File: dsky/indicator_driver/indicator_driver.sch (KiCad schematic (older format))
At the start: 0 parts

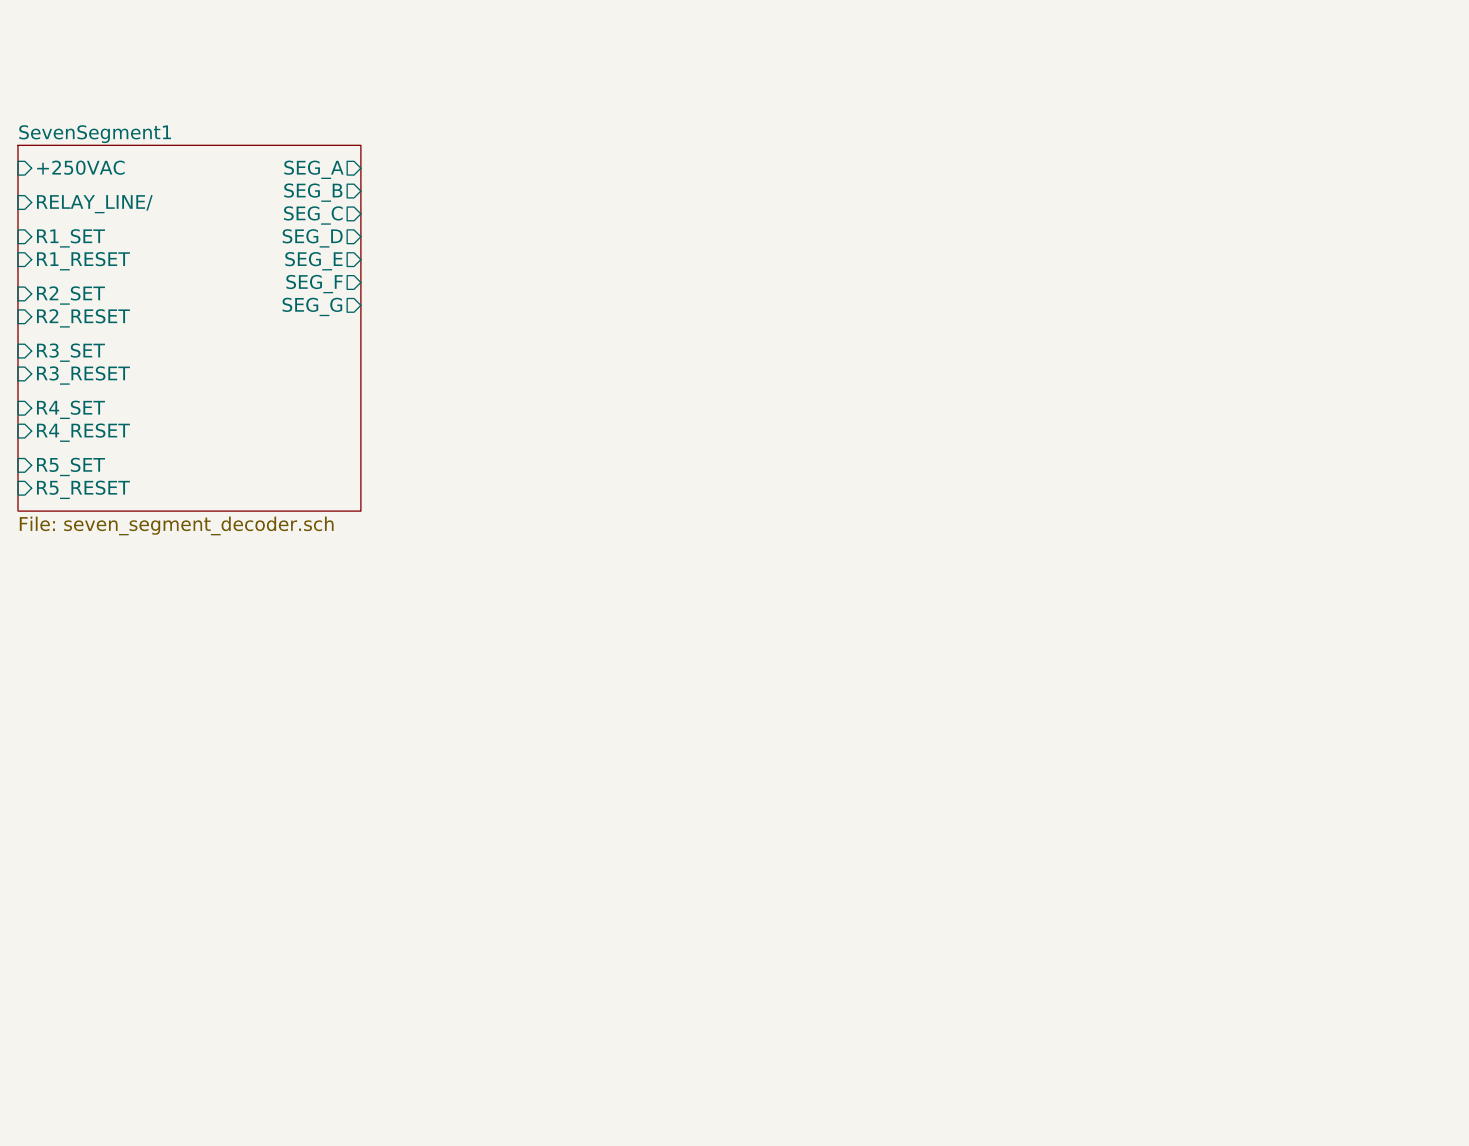
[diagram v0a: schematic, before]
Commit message: New (original) seven-segment decoder, taken from the Apollo 12 Mission Report
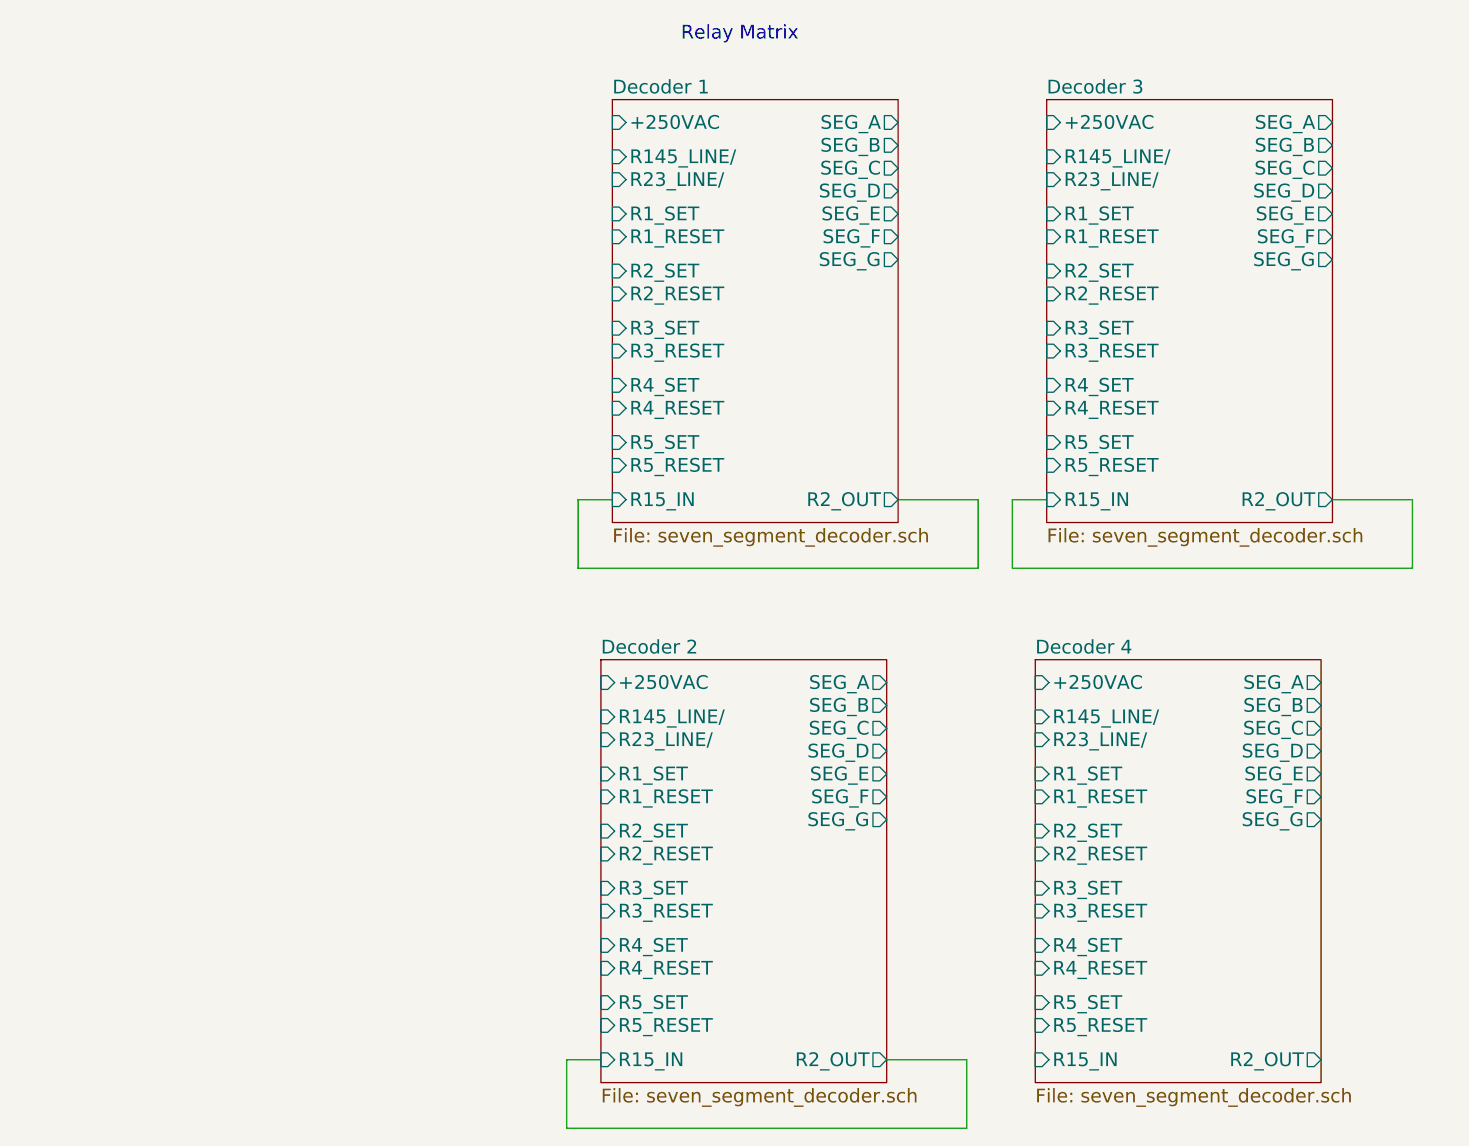
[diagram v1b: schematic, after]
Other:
- note added: "Relay Matrix"
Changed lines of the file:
@@
 $Descr A4 11693 8268
 encoding utf-8
-Sheet 1 2
+Sheet 1 5
 Title ""
 Date ""
@@
 $EndDescr
 $Sheet
-S 1650 1150 1500 1600
+S 4250 950  1250 1850
 U 57369BCB
-F0 "SevenSegment1" 60
+F0 "Decoder 1" 60
 F1 "seven_segment_decoder.sch" 60
-F2 "+250VAC" I L 1650 1250 60
-F3 "SEG_A" O R 3150 1250 60
-F4 "SEG_B" O R 3150 1350 60
-F5 "SEG_D" O R 3150 1550 60
-F6 "SEG_G" O R 3150 1850 60
-F7 "SEG_F" O R 3150 1750 60
-F8 "SEG_C" O R 3150 1450 60
-F9 "SEG_E" O R 3150 1650 60
-F10 "R5_SET" I L 1650 2550 60
-F11 "R5_RESET" I L 1650 2650 60
-F12 "R4_SET" I L 1650 2300 60
-F13 "R4_RESET" I L 1650 2400 60
-F14 "R3_SET" I L 1650 2050 60
-F15 "R3_RESET" I L 1650 2150 60
-F16 "R2_SET" I L 1650 1800 60
-F17 "R2_RESET" I L 1650 1900 60
-F18 "R1_SET" I L 1650 1550 60
-F19 "R1_RESET" I L 1650 1650 60
-F20 "RELAY_LINE/" I L 1650 1400 60
+F2 "+250VAC" I L 4250 1050 60
+F3 "SEG_A" O R 5500 1050 60
+F4 "SEG_B" O R 5500 1150 60
+F5 "SEG_D" O R 5500 1350 60
+F6 "SEG_G" O R 5500 1650 60
+F7 "SEG_F" O R 5500 1550 60
+F8 "SEG_C" O R 5500 1250 60
+F9 "SEG_E" O R 5500 1450 60
+F10 "R5_SET" I L 4250 2450 60
+F11 "R5_RESET" I L 4250 2550 60
+F12 "R4_SET" I L 4250 2200 60
+F13 "R4_RESET" I L 4250 2300 60
+F14 "R3_SET" I L 4250 1950 60
+F15 "R3_RESET" I L 4250 2050 60
+F16 "R2_SET" I L 4250 1700 60
+F17 "R2_RESET" I L 4250 1800 60
+F18 "R1_SET" I L 4250 1450 60
+F19 "R1_RESET" I L 4250 1550 60
+F20 "R145_LINE/" I L 4250 1200 60
+F21 "R23_LINE/" I L 4250 1300 60
+F22 "R2_OUT" O R 5500 2700 60
+F23 "R15_IN" I L 4250 2700 60
+$EndSheet
+Wire Wire Line
+	5500 2700 5850 2700
+Wire Wire Line
+	5850 2700 5850 3000
+Wire Wire Line
+	5850 3000 4100 3000
+Wire Wire Line
+	4100 3000 4100 2700
+Wire Wire Line
+	4100 2700 4250 2700
+Text Notes 4550 700  0    60   ~ 0
+Relay Matrix
+$Sheet
+S 4200 3400 1250 1850
+U 5823C123
+F0 "Decoder 2" 60
+F1 "seven_segment_decoder.sch" 60
+F2 "+250VAC" I L 4200 3500 60
+F3 "SEG_A" O R 5450 3500 60
+F4 "SEG_B" O R 5450 3600 60
+F5 "SEG_D" O R 5450 3800 60
+F6 "SEG_G" O R 5450 4100 60
+F7 "SEG_F" O R 5450 4000 60
+F8 "SEG_C" O R 5450 3700 60
+F9 "SEG_E" O R 5450 3900 60
+F10 "R5_SET" I L 4200 4900 60
+F11 "R5_RESET" I L 4200 5000 60
+F12 "R4_SET" I L 4200 4650 60
+F13 "R4_RESET" I L 4200 4750 60
+F14 "R3_SET" I L 4200 4400 60
+F15 "R3_RESET" I L 4200 4500 60
+F16 "R2_SET" I L 4200 4150 60
+F17 "R2_RESET" I L 4200 4250 60
+F18 "R1_SET" I L 4200 3900 60
+F19 "R1_RESET" I L 4200 4000 60
+F20 "R145_LINE/" I L 4200 3650 60
+F21 "R23_LINE/" I L 4200 3750 60
+F22 "R2_OUT" O R 5450 5150 60
+F23 "R15_IN" I L 4200 5150 60
+$EndSheet
+Wire Wire Line
+	5450 5150 5800 5150
+Wire Wire Line
+	5800 5150 5800 5450
+Wire Wire Line
+	5800 5450 4050 5450
+Wire Wire Line
+	4050 5450 4050 5150
+Wire Wire Line
+	4050 5150 4200 5150
+$Sheet
+S 6150 950  1250 1850
+U 582563A0
+F0 "Decoder 3" 60
+F1 "seven_segment_decoder.sch" 60
+F2 "+250VAC" I L 6150 1050 60
+F3 "SEG_A" O R 7400 1050 60
+F4 "SEG_B" O R 7400 1150 60
+F5 "SEG_D" O R 7400 1350 60
+F6 "SEG_G" O R 7400 1650 60
+F7 "SEG_F" O R 7400 1550 60
+F8 "SEG_C" O R 7400 1250 60
+F9 "SEG_E" O R 7400 1450 60
+F10 "R5_SET" I L 6150 2450 60
+F11 "R5_RESET" I L 6150 2550 60
+F12 "R4_SET" I L 6150 2200 60
+F13 "R4_RESET" I L 6150 2300 60
+F14 "R3_SET" I L 6150 1950 60
+F15 "R3_RESET" I L 6150 2050 60
+F16 "R2_SET" I L 6150 1700 60
+F17 "R2_RESET" I L 6150 1800 60
+F18 "R1_SET" I L 6150 1450 60
+F19 "R1_RESET" I L 6150 1550 60
+F20 "R145_LINE/" I L 6150 1200 60
+F21 "R23_LINE/" I L 6150 1300 60
+F22 "R2_OUT" O R 7400 2700 60
+F23 "R15_IN" I L 6150 2700 60
+$EndSheet
+Wire Wire Line
+	7400 2700 7750 2700
+Wire Wire Line
+	7750 2700 7750 3000
+Wire Wire Line
+	7750 3000 6000 3000
+Wire Wire Line
+	6000 3000 6000 2700
+Wire Wire Line
+	6000 2700 6150 2700
+$Sheet
+S 6100 3400 1250 1850
+U 582563BD
+F0 "Decoder 4" 60
+F1 "seven_segment_decoder.sch" 60
+F2 "+250VAC" I L 6100 3500 60
+F3 "SEG_A" O R 7350 3500 60
+F4 "SEG_B" O R 7350 3600 60
+F5 "SEG_D" O R 7350 3800 60
+F6 "SEG_G" O R 7350 4100 60
+F7 "SEG_F" O R 7350 4000 60
+F8 "SEG_C" O R 7350 3700 60
+F9 "SEG_E" O R 7350 3900 60
+F10 "R5_SET" I L 6100 4900 60
+F11 "R5_RESET" I L 6100 5000 60
+F12 "R4_SET" I L 6100 4650 60
+F13 "R4_RESET" I L 6100 4750 60
+F14 "R3_SET" I L 6100 4400 60
+F15 "R3_RESET" I L 6100 4500 60
+F16 "R2_SET" I L 6100 4150 60
+F17 "R2_RESET" I L 6100 4250 60
+F18 "R1_SET" I L 6100 3900 60
+F19 "R1_RESET" I L 6100 4000 60
+F20 "R145_LINE/" I L 6100 3650 60
+F21 "R23_LINE/" I L 6100 3750 60
+F22 "R2_OUT" O R 7350 5150 60
+F23 "R15_IN" I L 6100 5150 60
 $EndSheet
 $EndSCHEMATC

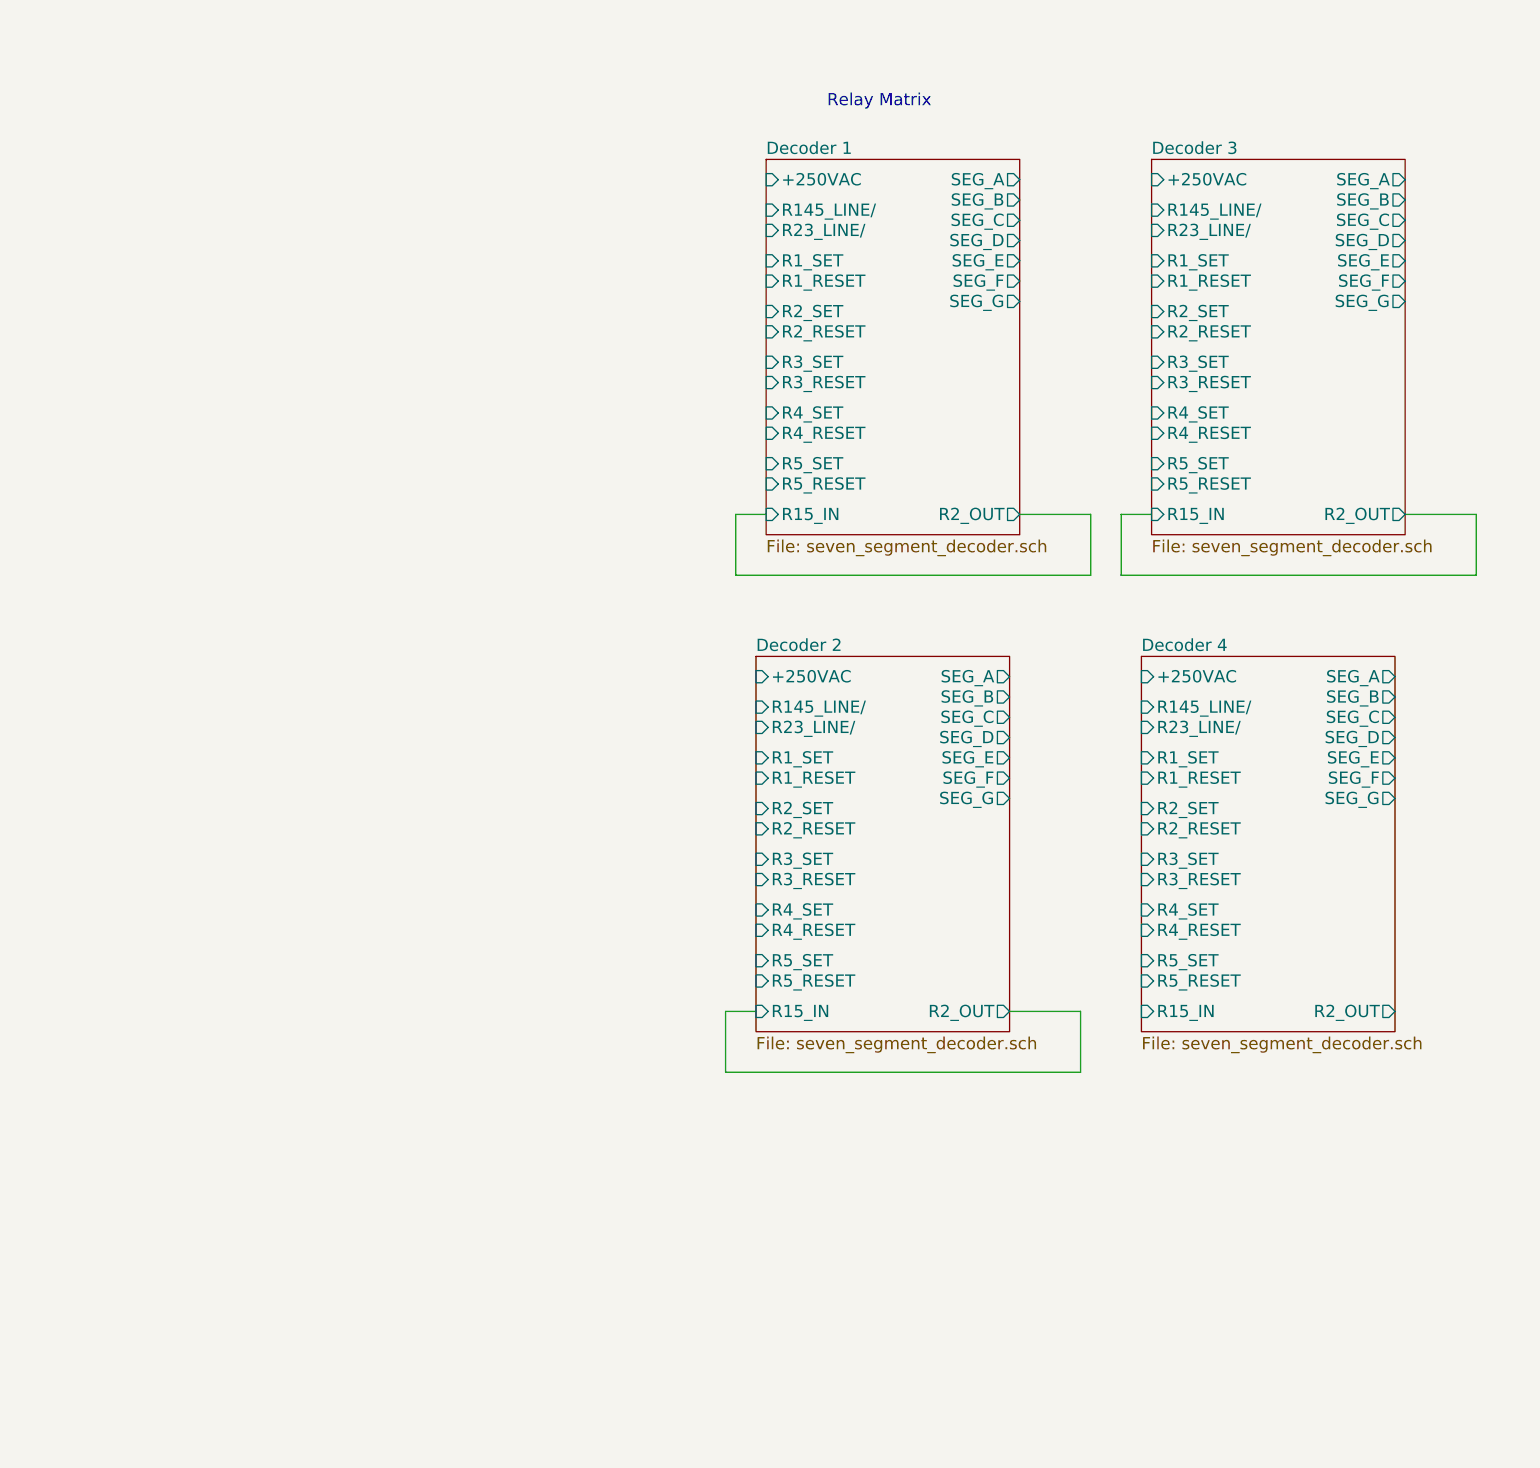
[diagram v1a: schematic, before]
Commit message: Added in the rest of the IDM hardware. Values and diode matrix design still need to be finalized. Working on wiring everything up now.
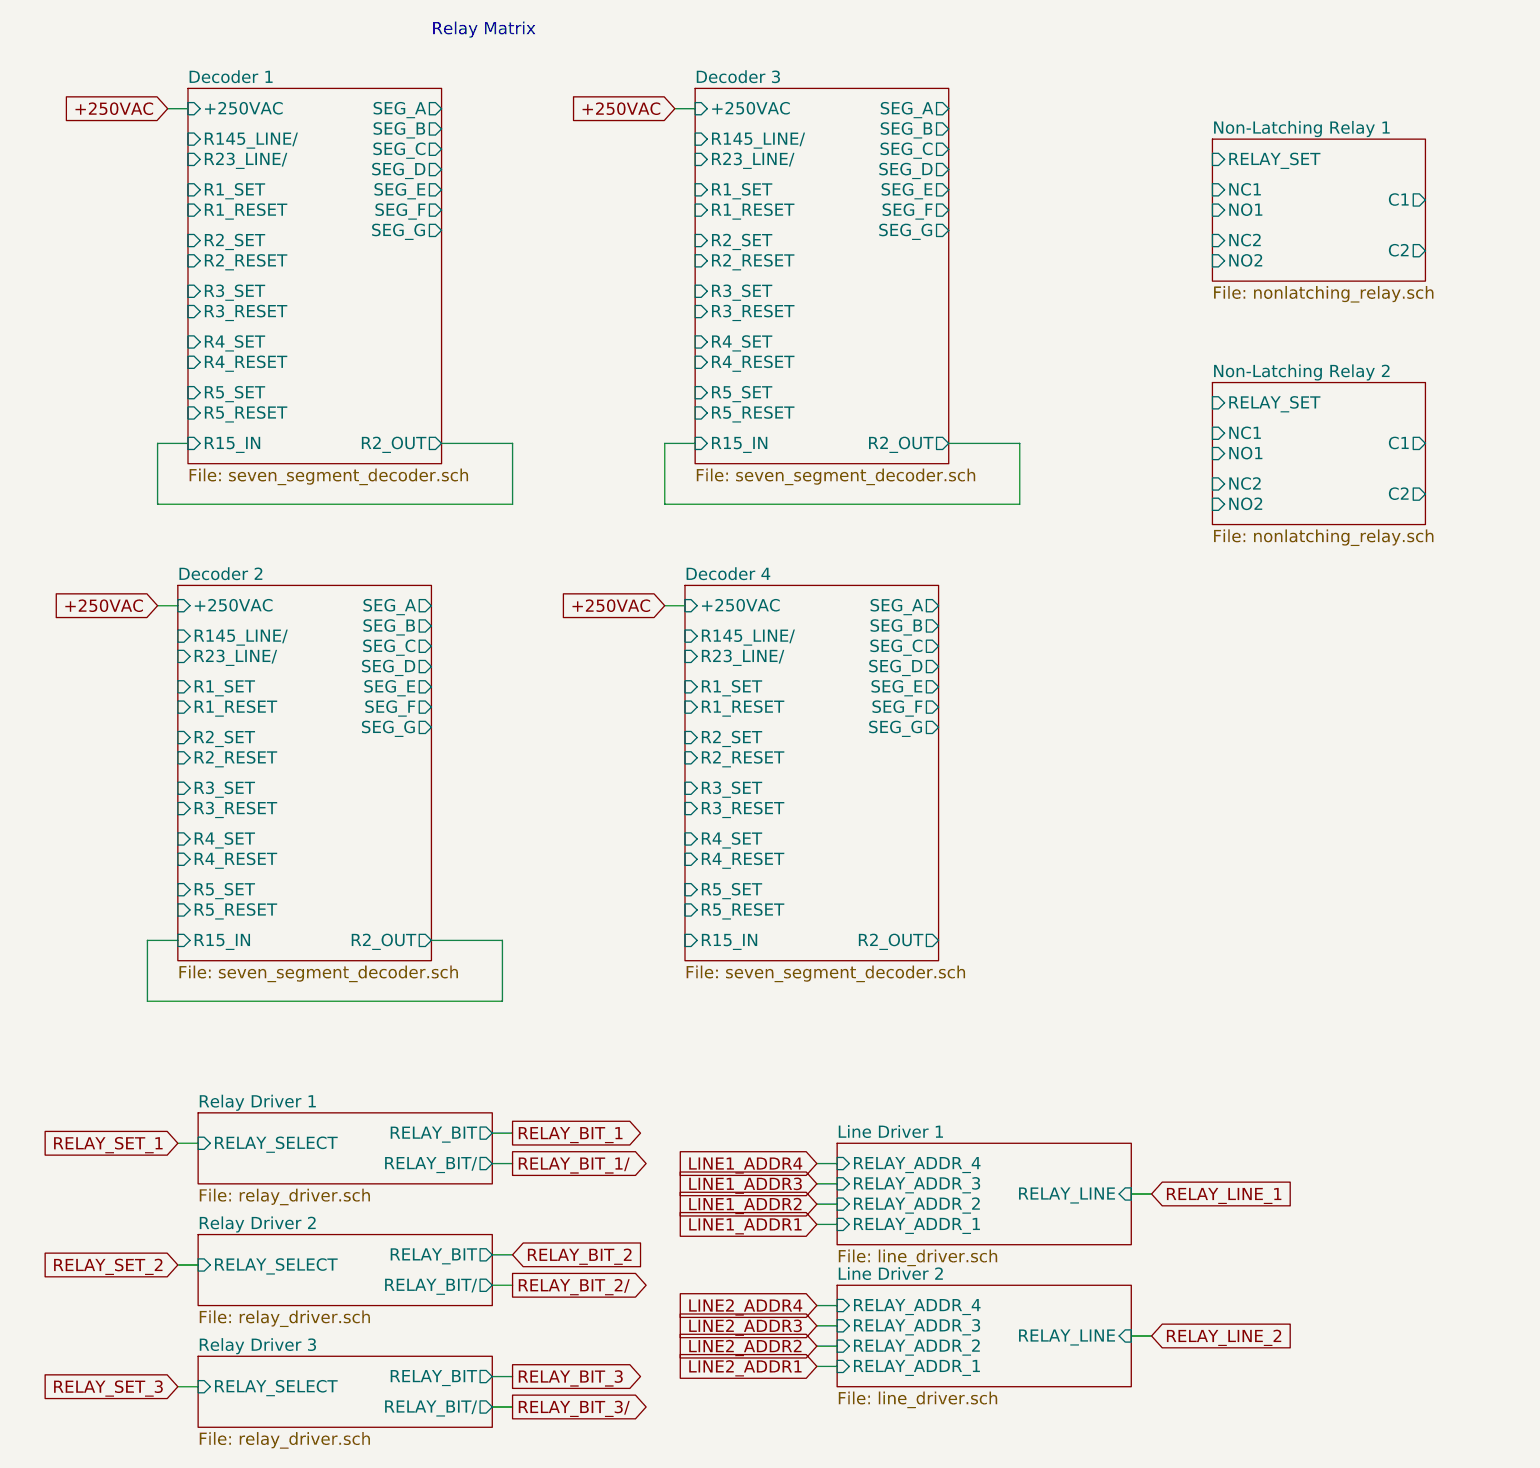
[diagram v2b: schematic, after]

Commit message: Finished initial wiring of the Indicator Driver Module. Currently sitting at 111 pins used, so I've been too aggressive at culling pins
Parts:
- added P1: DIN_41612_128P, symbol DIN_41612_128P
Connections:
- net labels added: +12V, DEC12_LINE/, DEC1_R1_R, DEC1_R1_S, DEC1_R2_R, DEC1_R2_S, DEC1_R3_R, DEC1_R3_S, DEC1_R4_R, DEC1_R4_S, DEC1_R5_R, DEC1_R5_S, DEC1_SEGA, DEC1_SEGB, DEC1_SEGC, DEC1_SEGD, DEC1_SEGE, DEC1_SEGF, DEC1_SEGG, DEC2_R1_R, DEC2_R1_S, DEC2_R2_R, DEC2_R2_S, DEC2_R3_R, DEC2_R3_S, DEC2_R4_R, DEC2_R4_S, DEC2_R5_R, DEC2_R5_S, DEC2_SEGA, DEC2_SEGB, DEC2_SEGC, DEC2_SEGD, DEC2_SEGE, DEC2_SEGF, DEC2_SEGG, DEC3_LINE/, DEC3_R1_R, DEC3_R1_S, DEC3_R2_R, DEC3_R2_S, DEC3_R3_R, DEC3_R3_S, DEC3_R4_R, DEC3_R4_S, DEC3_R5_R, DEC3_R5_S, DEC3_SEGA, DEC3_SEGB, DEC3_SEGC, DEC3_SEGD, DEC3_SEGE, DEC3_SEGF, DEC3_SEGG, DEC4_LINE145/, DEC4_LINE2/, DEC4_LINE3/, DEC4_R15_IN, DEC4_R1_R, DEC4_R1_S, DEC4_R2_OUT, DEC4_R2_R, DEC4_R2_S, DEC4_R3_R, DEC4_R3_S, DEC4_R4_R, DEC4_R4_S, DEC4_R5_R, DEC4_R5_S, DEC4_SEGA, DEC4_SEGB, DEC4_SEGC, DEC4_SEGD, DEC4_SEGE, DEC4_SEGF, DEC4_SEGG, GND, R21_C1, R21_C2, R21_NC1, R21_NC2, R21_NO1, R21_NO2, R21_S, R22_C1, R22_C2, R22_NC1, R22_NC2, R22_NO1, R22_NO2, R22_S
- wire segments 38 -> 141
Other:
- note added: "Line Drivers"
- note added: "Relay Drivers"
